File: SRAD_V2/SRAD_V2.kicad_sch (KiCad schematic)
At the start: 71 parts, among them J1 Conn_01x04_Pin, J3 RSP-122811-02, J4 USB_C_Receptacle_USB2.0_16P, J6 691210910002, J7 691210910002, Q6 MMBT3904, U1 STM32F767ZIT6, U12 MAX-M10S, U13 MS5607-02BA, U14 MMC5983MA, U17 AS5F31G04SND-08LIN, U5 LSM6DSVTR, X1 Crystal

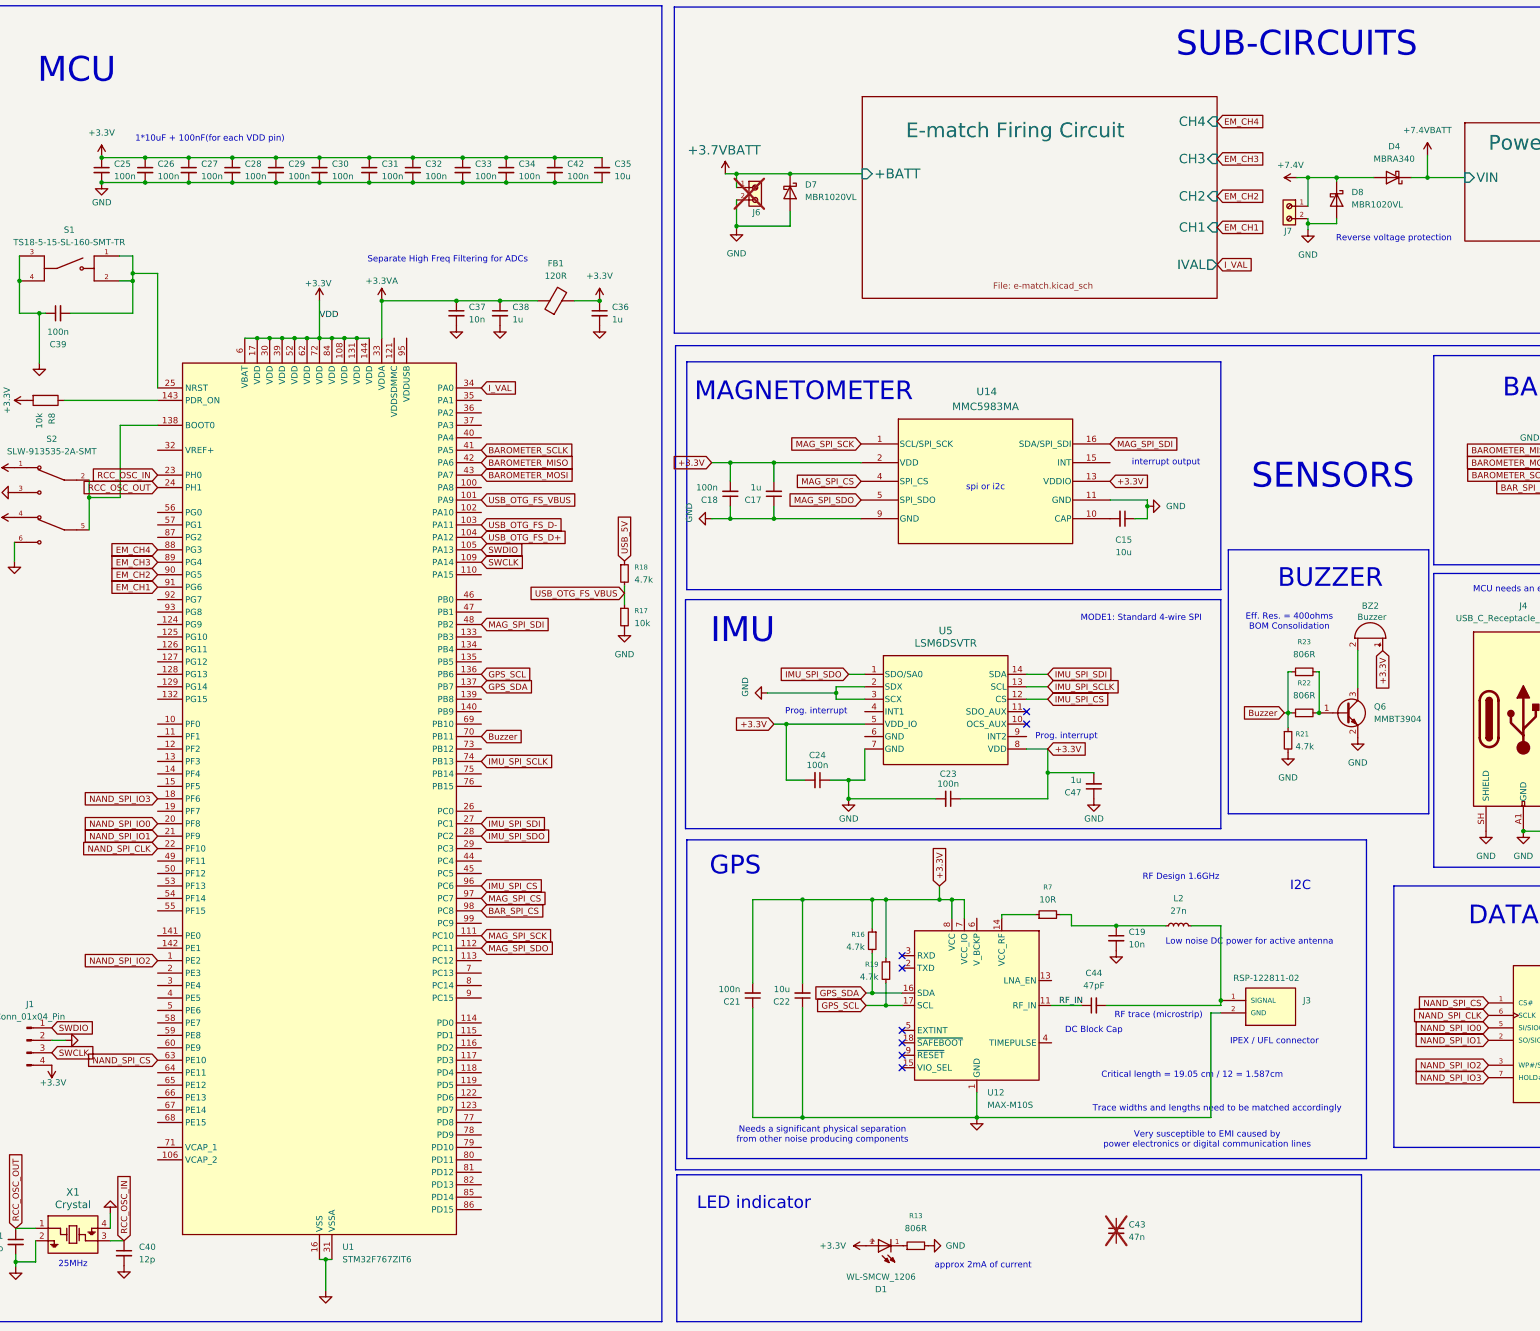
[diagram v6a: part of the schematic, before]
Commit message: Added the JST connectors
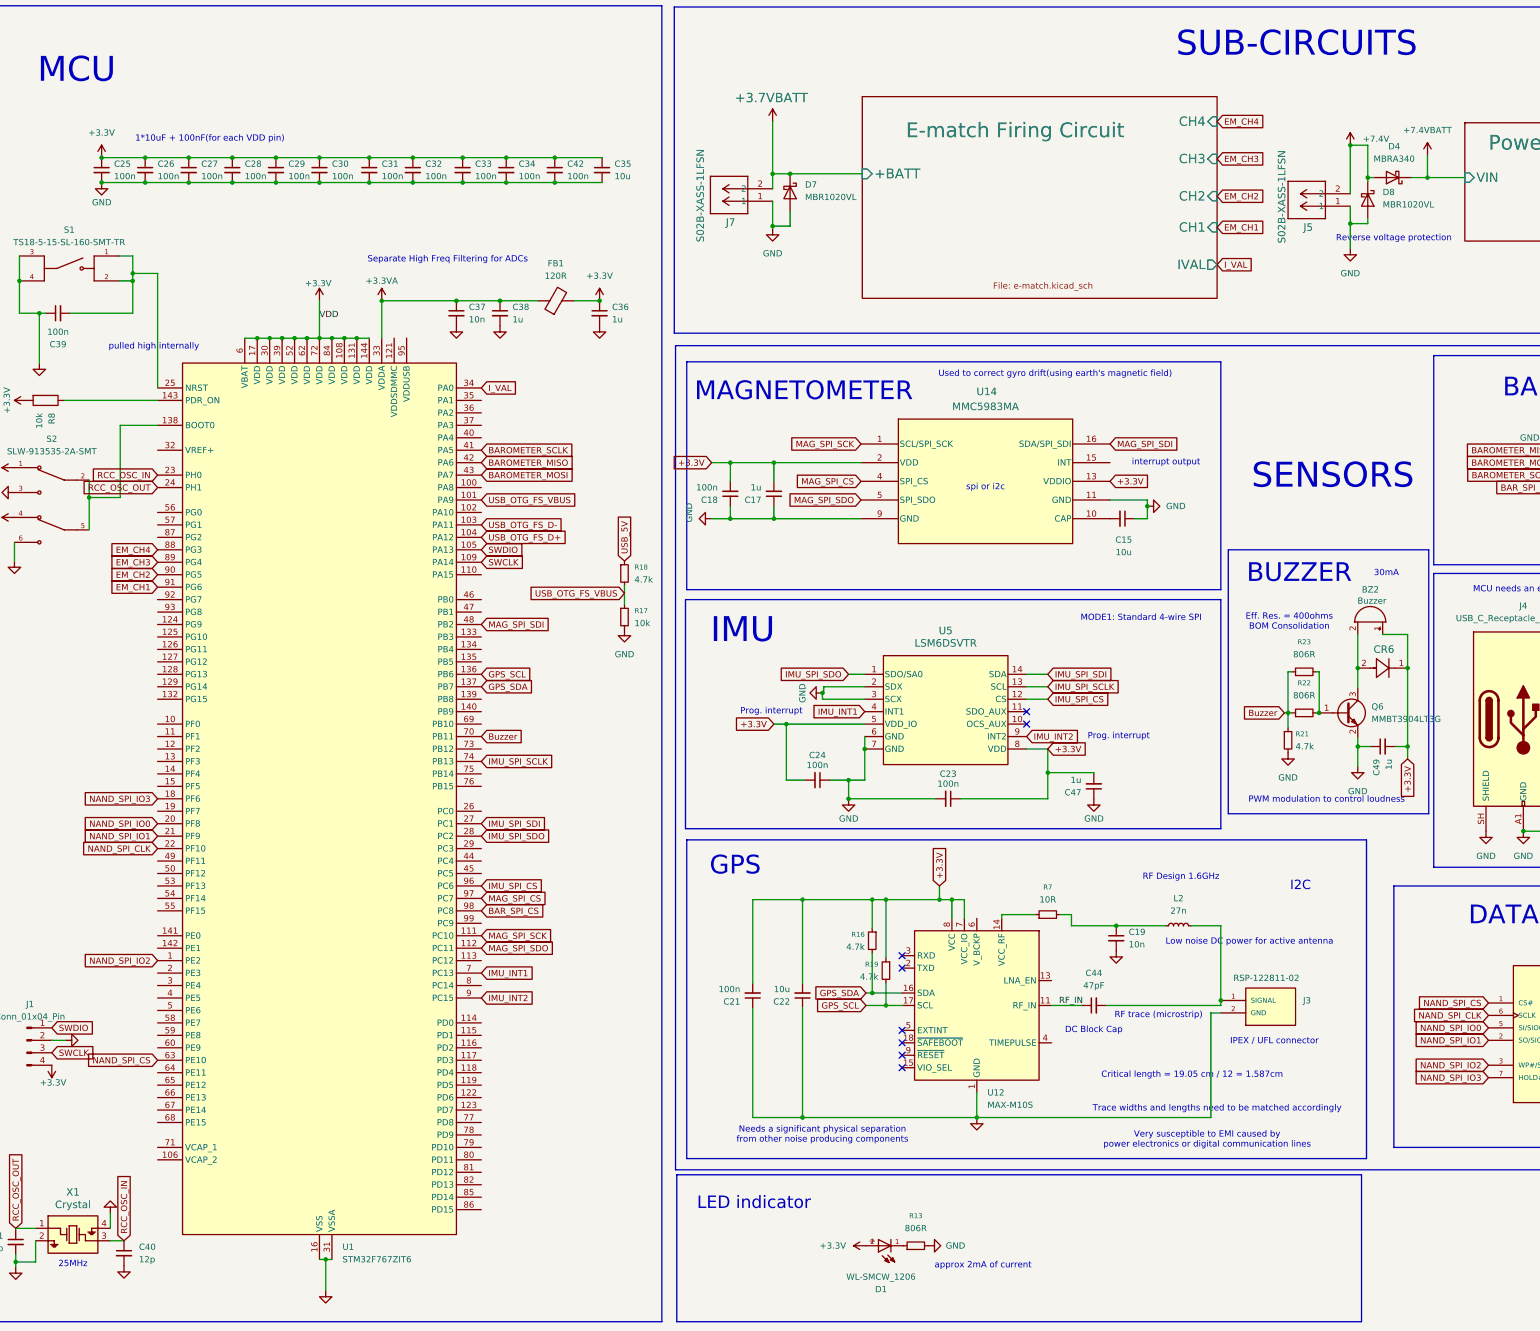
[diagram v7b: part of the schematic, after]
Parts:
- removed C43: 47n, Capacitor_SMD:C_0402_1005Metric, symbol Device:C_Small
- removed J6, J7: 691210910002, Screw_Terminal:691210910002, symbol Screw Terminal:691210910002
- added C49: 1u, Capacitor_SMD:C_0603_1608Metric, symbol Device:C_Small
- added CR6: MSS1P5-M3/89A, Schottky_Diode:DIODE_MSP3V3, symbol Schottcky Diode:MSS1P5-M3_89A
- added J5, J7: S02B-XASS-1LFSN, S02B-XASS-1:CONN2_S02B-XASS_295x496_JST, symbol S02B-XASS-1:S02B-XASS-1LFSN
- C37: footprint Capacitor_SMD:C_0402_1005Metric_Pad0.74x0.62mm_HandSolder -> Resistor_SMD:R_0402_1005Metric
- Q6: value MMBT3904 -> MMBT3904LT3G
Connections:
- net +3.3V: now also C49.2, CR6.1
- net +3.7VBATT: now also J7.2
- net +7.4V: now also J5.2
- net GND: now also U5.6 (GND), C49.1, J5.1, J7.1
- net at BZ2.2 (-), Q6.3 (C): now also CR6.2
- net IMU_INT1: now reaches U1.7 (PC13)
- net IMU_INT1: now also U5.4 (INT1)
- net IMU_INT2: now reaches U1.9 (PC15)
- net IMU_INT2: now also U5.9 (INT2)
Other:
- note added: "30mA"
- note added: "PWM modulation to control loudness"
- note added: "Used to correct gyro drift(using earth's magnetic field)"
- note added: "pulled high internally"
- moved on the sheet: BZ2, D8

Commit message: Creating a Fab drawing
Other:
- note added: "Bidirectional TVS diode"
- note added: "Reverse voltage protection + TVS"
- note removed: "Reverse voltage protection"
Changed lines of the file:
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@@
 		)
 	)
-	(text "Reverse voltage protection"
+	(text "Reverse voltage protection + TVS"
 		(exclude_from_sim no)
-		(at 304.292 60.96 0)
+		(at 304.292 71.12 0)
 		(effects
 			(font
@@
 		(effects
 			(font
+				(size 1.27 1.27)
+			)
+		)
+	)
+	(text "Bidirectional TVS diode"
+		(exclude_from_sim no)
+		(at 182.118 70.358 0)
+		(effects
+			(font
